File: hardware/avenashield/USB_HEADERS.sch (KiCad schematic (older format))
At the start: 1 part, among them J5 USB Headers Board Top

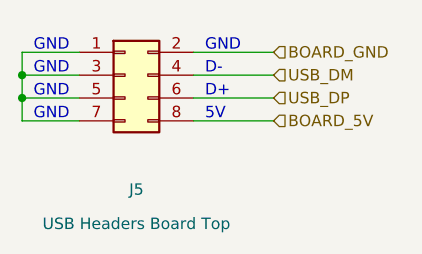
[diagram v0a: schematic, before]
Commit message: Added MiniPCIe latch clip and replaced onboard LEDs with connector
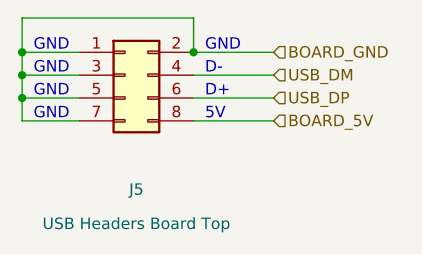
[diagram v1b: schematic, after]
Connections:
- net BOARD_GND: now also J5.1 (Pin_1), J5.3 (Pin_3), J5.5 (Pin_5), J5.7 (Pin_7)
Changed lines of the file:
@@
 $Descr A4 11693 8268
 encoding utf-8
-Sheet 7 7
+Sheet 5 7
 Title ""
 Date ""
@@
 Wire Wire Line
 	4450 2250 4800 2250
+Connection ~ 3700 1950
+Wire Wire Line
+	3700 1800 4450 1800
+Wire Wire Line
+	4450 1800 4450 1950
+Wire Wire Line
+	3700 1800 3700 1950
+Connection ~ 4450 1950
 $EndSCHEMATC

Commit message: Improved I2C bus routing
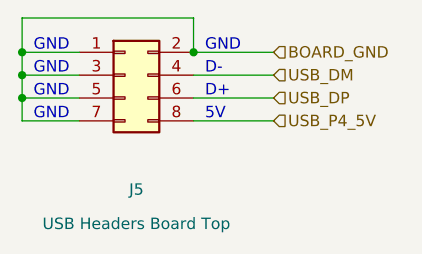
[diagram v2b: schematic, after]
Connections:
- net BOARD_5V renamed USB_P4_5V
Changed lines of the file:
@@
 	4800 2150 4450 2150
 Text HLabel 4800 2250 2    50   Input ~ 0
-BOARD_5V
+USB_P4_5V
 Text HLabel 4800 1950 2    50   Input ~ 0
 BOARD_GND
